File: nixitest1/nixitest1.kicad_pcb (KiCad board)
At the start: 2 copper layers, 22 x 38 mm, 32 parts, among them J1 MSYS, Q1 60V 3A, Q10 HVN, Q11 HVN, Q12 HVN, Q13 HVN, Q2 HVN, Q3 HVN, Q4 HVN, Q5 HVN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

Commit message: Update board design
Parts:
- R1: value 500mΩ -> 10k; footprint Resistor_SMD:R_0805_2012Metric -> Resistor_SMD:R_0402_1005Metric
- moved R1 1.36 mm to (89.0, 65.2), turned to 180 degrees
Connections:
- Q1 pad 2: HVIMON -> GND
- R1 pad 1: HVIMON -> GND
- R1 pad 2: GND -> HVCTL
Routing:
- net HVIMON: track 12.9 -> 0.51 mm, vias 2 -> 0
- net GND: track 172.8 -> 181.8 mm
- net HVCTL: track 7.85 -> 8.91 mm
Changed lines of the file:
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@@
     )
   )
-  (footprint "Resistor_SMD:R_0805_2012Metric" (layer "F.Cu")
-    (at 90.29 64.88)
-    (descr "Resistor SMD 0805 (2012 Metric), square (rectangular) end terminal, IPC_7351 nominal, (Body size source: IPC-SM-782 page 72, https://www.pcb-3d.com/wordpress/wp-content/uploads/ipc-sm-782a_amendment_1_and_2.pdf), generated with kicad-footprint-generator")
+  (footprint "Resistor_SMD:R_0402_1005Metric" (layer "F.Cu")
+    (at 88.97 65.19 180)
+    (descr "Resistor SMD 0402 (1005 Metric), square (rectangular) end terminal, IPC_7351 nominal, (Body size source: IPC-SM-782 page 72, https://www.pcb-3d.com/wordpress/wp-content/uploads/ipc-sm-782a_amendment_1_and_2.pdf), generated with kicad-footprint-generator")
     (tags "resistor")
-    (property "LCSC" "C327217")
-    (property "Sheetfile" "nixitest1.kicad_sch")
-    (property "Sheetname" "")
-    (attr smd)
-    (fp_text reference "R1" (at -2.38 -0.48 unlocked) (layer "F.SilkS")
-      (effects (font (size 0.7 0.7) (thickness 0.1)))
-    )
-    (fp_text value "500mΩ" (at 0 1.65 unlocked) (layer "F.Fab")
+    (property "LCSC" "C25744")
+    (property "Sheetfile" "nixitest1.kicad_sch")
+    (property "Sheetname" "")
+    (attr smd)
+    (fp_text reference "R1" (at -1.73 0.03 unlocked) (layer "F.SilkS")
+      (effects (font (size 0.7 0.7) (thickness 0.1)))
+    )
+    (fp_text value "10k" (at 0 1.17 unlocked) (layer "F.Fab")
       (effects (font (size 1 1) (thickness 0.15)))
     )
@@
       (effects (font (size 1 1) (thickness 0.15)))
     )
-    (fp_line (start -0.227064 -0.735) (end 0.227064 -0.735) (layer "F.SilkS") (width 0.1))
-    (fp_line (start -0.227064 0.735) (end 0.227064 0.735) (layer "F.SilkS") (width 0.1))
-    (fp_line (start -1.68 0.95) (end -1.68 -0.95) (layer "F.CrtYd") (width 0.05))
-    (fp_line (start -1.68 -0.95) (end 1.68 -0.95) (layer "F.CrtYd") (width 0.05))
-    (fp_line (start 1.68 -0.95) (end 1.68 0.95) (layer "F.CrtYd") (width 0.05))
-    (fp_line (start 1.68 0.95) (end -1.68 0.95) (layer "F.CrtYd") (width 0.05))
-    (fp_line (start -1 0.625) (end -1 -0.625) (layer "F.Fab") (width 0.1))
-    (fp_line (start 1 -0.625) (end 1 0.625) (layer "F.Fab") (width 0.1))
-    (fp_line (start 1 0.625) (end -1 0.625) (layer "F.Fab") (width 0.1))
-    (fp_line (start -1 -0.625) (end 1 -0.625) (layer "F.Fab") (width 0.1))
-    (pad "1" smd roundrect locked (at -0.9125 0) (size 1.025 1.4) (layers "F.Cu" "F.Paste" "F.Mask") (roundrect_rratio 0.243902439)
-      (net 5 "HVIMON") (pintype "passive"))
-    (pad "2" smd roundrect locked (at 0.9125 0) (size 1.025 1.4) (layers "F.Cu" "F.Paste" "F.Mask") (roundrect_rratio 0.243902439)
+    (fp_line (start -0.153641 -0.38) (end 0.153641 -0.38) (layer "F.SilkS") (width 0.1))
+    (fp_line (start -0.153641 0.38) (end 0.153641 0.38) (layer "F.SilkS") (width 0.1))
+    (fp_line (start 0.93 0.47) (end -0.93 0.47) (layer "F.CrtYd") (width 0.05))
+    (fp_line (start 0.93 -0.47) (end 0.93 0.47) (layer "F.CrtYd") (width 0.05))
+    (fp_line (start -0.93 -0.47) (end 0.93 -0.47) (layer "F.CrtYd") (width 0.05))
+    (fp_line (start -0.93 0.47) (end -0.93 -0.47) (layer "F.CrtYd") (width 0.05))
+    (fp_line (start 0.525 0.27) (end -0.525 0.27) (layer "F.Fab") (width 0.1))
+    (fp_line (start 0.525 -0.27) (end 0.525 0.27) (layer "F.Fab") (width 0.1))
+    (fp_line (start -0.525 -0.27) (end 0.525 -0.27) (layer "F.Fab") (width 0.1))
+    (fp_line (start -0.525 0.27) (end -0.525 -0.27) (layer "F.Fab") (width 0.1))
+    (pad "1" smd roundrect (at -0.51 0 180) (size 0.54 0.64) (layers "F.Cu" "F.Paste" "F.Mask") (roundrect_rratio 0.25)
       (net 2 "GND") (pintype "passive"))
-    (model "${KICAD6_3DMODEL_DIR}/Resistor_SMD.3dshapes/R_0805_2012Metric.wrl"
+    (pad "2" smd roundrect (at 0.51 0 180) (size 0.54 0.64) (layers "F.Cu" "F.Paste" "F.Mask") (roundrect_rratio 0.25)
+      (net 4 "HVCTL") (pintype "passive"))
+    (model "${KICAD6_3DMODEL_DIR}/Resistor_SMD.3dshapes/R_0402_1005Metric.wrl"
       (offset (xyz 0 0 0))
       (scale (xyz 1 1 1))
@@
       (net 4 "HVCTL") (pinfunction "G") (pintype "input"))
     (pad "2" smd roundrect (at -0.9375 0.95) (size 1.475 0.6) (layers "F.Cu" "F.Paste" "F.Mask") (roundrect_rratio 0.25)
-      (net 5 "HVIMON") (pinfunction "S") (pintype "passive"))
+      (net 2 "GND") (pinfunction "S") (pintype "passive"))
     (pad "3" smd roundrect (at 0.9375 0) (size 1.475 0.6) (layers "F.Cu" "F.Paste" "F.Mask") (roundrect_rratio 0.25)
       (net 6 "Net-(Q1-Pad3)") (pinfunction "D") (pintype "passive"))
@@
   (footprint "IN12-NIXIE:IN12-NIXIE" (layer "F.Cu")
     (at 90 80)
-    (property "LCSC" "~")
+    (property "LCSC" "")
     (property "Sheetfile" "nixitest1.kicad_sch")
     (property "Sheetname" "")
@@
   (gr_arc (start 99 58) (mid 100.414214 58.585786) (end 101 60) (layer "Edge.Cuts") (width 0.1))
   (gr_text "*" (at 87.42 71.84 -120) (layer "B.SilkS")
-    (effects (font (size 1.5 1.5) (thickness 0.15)) (justify mirror))
+    (effects (font (size 0.7 0.7) (thickness 0.1)) (justify mirror))
   )
   (gr_text "GND" (at 85.26 94.31) (layer "F.SilkS")
@@
   )
   (gr_text "*" (at 88.175 71.75 120) (layer "F.SilkS")
-    (effects (font (size 1.5 1.5) (thickness 0.15)))
+    (effects (font (size 0.7 0.7) (thickness 0.1)))
   )
   (gr_text "PGM" (at 94.81 94.35) (layer "F.SilkS")
@@
   (segment (start 82.6 70.975) (end 83.95 71.175) (width 0.2) (layer "F.Cu") (net 2))
   (segment (start 91.307459 58.332541) (end 88.801628 58.328372) (width 0.2) (layer "F.Cu") (net 2))
+  (segment (start 89.48 65.19) (end 90.34 65.33) (width 0.2) (layer "F.Cu") (net 2))
   (segment (start 87.98 82.51) (end 88.2875 84.99) (width 0.2) (layer "F.Cu") (net 2))
   (segment (start 84.925 78.725) (end 85.525 79.225) (width 0.2) (layer "F.Cu") (net 2))
@@
   (segment (start 81.67 81.33) (end 80.925 80.85) (width 0.2) (layer "F.Cu") (net 2))
   (segment (start 84.79 64.075) (end 85.09 63.8) (width 0.2) (layer "F.Cu") (net 2))
+  (segment (start 90.34 65.33) (end 90.65 66.75) (width 0.2) (layer "F.Cu") (net 2))
   (segment (start 93.25 67.15) (end 94.873855 67.098855) (width 0.2) (layer "F.Cu") (net 2))
+  (segment (start 90.65 66.75) (end 90.25 67.2) (width 0.2) (layer "F.Cu") (net 2))
   (segment (start 90.113482 76.523482) (end 91.67 76.35) (width 0.2) (layer "F.Cu") (net 2))
   (segment (start 93.77 85.88) (end 92.0025 85.74) (width 0.2) (layer "F.Cu") (net 2))
@@
   (segment (start 82.9 74.45) (end 82.76 75.32) (width 0.2) (layer "F.Cu") (net 2))
   (segment (start 82.91 75.96) (end 83.9758 78.4758) (width 0.2) (layer "F.Cu") (net 2))
+  (segment (start 90.25 67.2) (end 89.4625 68.5) (width 0.2) (layer "F.Cu") (net 2))
   (segment (start 97.61 79.51) (end 99.0575 81.02) (width 0.2) (layer "F.Cu") (net 2))
   (segment (start 83.52 73.28) (end 84.08 73.92) (width 0.2) (layer "F.Cu") (net 2))
@@
   (segment (start 91.28 58.83) (end 91.305749 58.325749) (width 0.2) (layer "B.Cu") (net 2))
   (segment (start 83.575 63.725) (end 83.225 63.35) (width 0.2) (layer "B.Cu") (net 2))
+  (segment (start 86.975 68.85) (end 85.1 67.25) (width 0.2) (layer "B.Cu") (net 2))
   (segment (start 87.33 63.6) (end 85.09 63.8) (width 0.2) (layer "B.Cu") (net 2))
   (segment (start 85.09 63.8) (end 83.575 63.725) (width 0.2) (layer "B.Cu") (net 2))
@@
   (segment (start 83.375 62.525) (end 84.925 61.65) (width 0.2) (layer "B.Cu") (net 2))
   (segment (start 85.95 66.55) (end 85.09 63.8) (width 0.2) (layer "B.Cu") (net 2))
+  (segment (start 84.825 67.175) (end 83.05 67.475) (width 0.2) (layer "B.Cu") (net 2))
   (segment (start 80.84 58.55) (end 84.67 58.31) (width 0.2) (layer "B.Cu") (net 2))
+  (segment (start 85.1 67.25) (end 84.825 67.175) (width 0.2) (layer "B.Cu") (net 2))
   (segment (start 83.225 63.35) (end 83.375 62.525) (width 0.2) (layer "B.Cu") (net 2))
   (segment (start 88.351263 58.318737) (end 91.305749 58.325749) (width 0.2) (layer "B.Cu") (net 2))
@@
   (segment (start 88.225 66.225) (end 89.4625 66.6) (width 0.2) (layer "F.Cu") (net 4))
   (segment (start 83.41 66.74) (end 83.02 66.81) (width 0.2) (layer "F.Cu") (net 4))
+  (segment (start 88.225 66.225) (end 88.46 65.19) (width 0.2) (layer "F.Cu") (net 4))
   (segment (start 83.909999 66.74) (end 83.41 66.74) (width 0.2) (layer "F.Cu") (net 4))
   (via (at 88.225 66.225) (size 0.5) (drill 0.25) (layers "F.Cu" "B.Cu") (net 4))
@@
   (segment (start 87.925 66.65) (end 88.225 66.225) (width 0.2) (layer "B.Cu") (net 4))
   (segment (start 85.75 67.125) (end 86.325 67.2) (width 0.2) (layer "B.Cu") (net 4))
-  (segment (start 89.3375 64.65) (end 90.65 65.85) (width 0.2) (layer "F.Cu") (net 5))
   (segment (start 83.909999 67.14) (end 83.4 67.15) (width 0.2) (layer "F.Cu") (net 5))
-  (segment (start 83.4 67.15) (end 83.05 67.475) (width 0.2) (layer "F.Cu") (net 5))
-  (segment (start 90.25 67.2) (end 89.4625 68.5) (width 0.2) (layer "F.Cu") (net 5))
-  (segment (start 86.975 68.85) (end 89.4625 68.5) (width 0.2) (layer "F.Cu") (net 5))
-  (segment (start 90.65 65.85) (end 90.65 66.75) (width 0.2) (layer "F.Cu") (net 5))
-  (segment (start 90.65 66.75) (end 90.25 67.2) (width 0.2) (layer "F.Cu") (net 5))
-  (via (at 83.05 67.475) (size 0.5) (drill 0.25) (layers "F.Cu" "B.Cu") (net 5))
-  (via (at 86.975 68.85) (size 0.5) (drill 0.25) (layers "F.Cu" "B.Cu") (net 5))
-  (segment (start 86.975 68.85) (end 85.1 67.25) (width 0.2) (layer "B.Cu") (net 5))
-  (segment (start 84.825 67.175) (end 83.05 67.475) (width 0.2) (layer "B.Cu") (net 5))
-  (segment (start 85.1 67.25) (end 84.825 67.175) (width 0.2) (layer "B.Cu") (net 5))
   (segment (start 91.3375 67.55) (end 93.065 68.9) (width 0.2) (layer "F.Cu") (net 6))
   (segment (start 85.66 78.42) (end 86.8875 78.62) (width 0.2) (layer "F.Cu") (net 7))

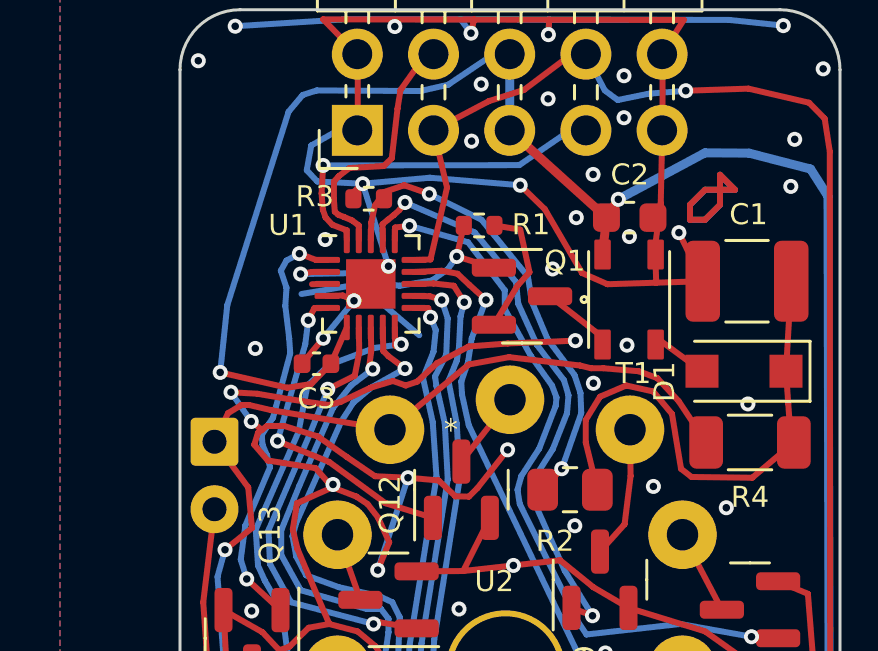
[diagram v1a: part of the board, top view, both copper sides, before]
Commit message: * Revert pcb so it matches production files. * Move original thoughts into attic. * Update comments on firmware
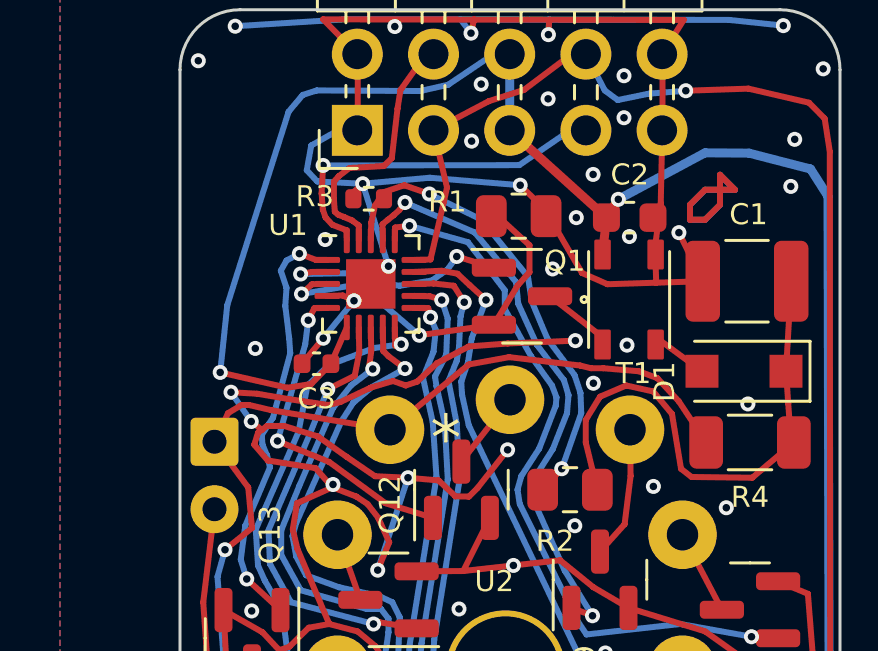
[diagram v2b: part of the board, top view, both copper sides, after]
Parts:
- R1: value 10k -> 500mΩ; footprint Resistor_SMD:R_0402_1005Metric -> Resistor_SMD:R_0805_2012Metric
- moved R1 1.36 mm to (90.3, 64.9), turned to 0 degrees
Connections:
- Q1 pad 2: GND -> HVIMON
- R1 pad 1: GND -> HVIMON
- R1 pad 2: HVCTL -> GND
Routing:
- net HVIMON: track 0.51 -> 12.9 mm, vias 0 -> 2
- net GND: track 181.8 -> 172.8 mm
- net HVCTL: track 8.91 -> 7.85 mm
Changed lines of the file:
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@@
     )
   )
-  (footprint "Resistor_SMD:R_0402_1005Metric" (layer "F.Cu")
-    (at 88.97 65.19 180)
-    (descr "Resistor SMD 0402 (1005 Metric), square (rectangular) end terminal, IPC_7351 nominal, (Body size source: IPC-SM-782 page 72, https://www.pcb-3d.com/wordpress/wp-content/uploads/ipc-sm-782a_amendment_1_and_2.pdf), generated with kicad-footprint-generator")
+  (footprint "Resistor_SMD:R_0805_2012Metric" (layer "F.Cu")
+    (at 90.29 64.88)
+    (descr "Resistor SMD 0805 (2012 Metric), square (rectangular) end terminal, IPC_7351 nominal, (Body size source: IPC-SM-782 page 72, https://www.pcb-3d.com/wordpress/wp-content/uploads/ipc-sm-782a_amendment_1_and_2.pdf), generated with kicad-footprint-generator")
     (tags "resistor")
-    (property "LCSC" "C25744")
-    (property "Sheetfile" "nixitest1.kicad_sch")
-    (property "Sheetname" "")
-    (attr smd)
-    (fp_text reference "R1" (at -1.73 0.03 unlocked) (layer "F.SilkS")
-      (effects (font (size 0.7 0.7) (thickness 0.1)))
-    )
-    (fp_text value "10k" (at 0 1.17 unlocked) (layer "F.Fab")
+    (property "LCSC" "C327217")
+    (property "Sheetfile" "nixitest1.kicad_sch")
+    (property "Sheetname" "")
+    (attr smd)
+    (fp_text reference "R1" (at -2.38 -0.48 unlocked) (layer "F.SilkS")
+      (effects (font (size 0.7 0.7) (thickness 0.1)))
+    )
+    (fp_text value "500mΩ" (at 0 1.65 unlocked) (layer "F.Fab")
       (effects (font (size 1 1) (thickness 0.15)))
     )
@@
       (effects (font (size 1 1) (thickness 0.15)))
     )
-    (fp_line (start -0.153641 -0.38) (end 0.153641 -0.38) (layer "F.SilkS") (width 0.1))
-    (fp_line (start -0.153641 0.38) (end 0.153641 0.38) (layer "F.SilkS") (width 0.1))
-    (fp_line (start 0.93 0.47) (end -0.93 0.47) (layer "F.CrtYd") (width 0.05))
-    (fp_line (start 0.93 -0.47) (end 0.93 0.47) (layer "F.CrtYd") (width 0.05))
-    (fp_line (start -0.93 -0.47) (end 0.93 -0.47) (layer "F.CrtYd") (width 0.05))
-    (fp_line (start -0.93 0.47) (end -0.93 -0.47) (layer "F.CrtYd") (width 0.05))
-    (fp_line (start 0.525 0.27) (end -0.525 0.27) (layer "F.Fab") (width 0.1))
-    (fp_line (start 0.525 -0.27) (end 0.525 0.27) (layer "F.Fab") (width 0.1))
-    (fp_line (start -0.525 -0.27) (end 0.525 -0.27) (layer "F.Fab") (width 0.1))
-    (fp_line (start -0.525 0.27) (end -0.525 -0.27) (layer "F.Fab") (width 0.1))
-    (pad "1" smd roundrect (at -0.51 0 180) (size 0.54 0.64) (layers "F.Cu" "F.Paste" "F.Mask") (roundrect_rratio 0.25)
+    (fp_line (start -0.227064 -0.735) (end 0.227064 -0.735) (layer "F.SilkS") (width 0.1))
+    (fp_line (start -0.227064 0.735) (end 0.227064 0.735) (layer "F.SilkS") (width 0.1))
+    (fp_line (start -1.68 0.95) (end -1.68 -0.95) (layer "F.CrtYd") (width 0.05))
+    (fp_line (start -1.68 -0.95) (end 1.68 -0.95) (layer "F.CrtYd") (width 0.05))
+    (fp_line (start 1.68 -0.95) (end 1.68 0.95) (layer "F.CrtYd") (width 0.05))
+    (fp_line (start 1.68 0.95) (end -1.68 0.95) (layer "F.CrtYd") (width 0.05))
+    (fp_line (start -1 0.625) (end -1 -0.625) (layer "F.Fab") (width 0.1))
+    (fp_line (start 1 -0.625) (end 1 0.625) (layer "F.Fab") (width 0.1))
+    (fp_line (start 1 0.625) (end -1 0.625) (layer "F.Fab") (width 0.1))
+    (fp_line (start -1 -0.625) (end 1 -0.625) (layer "F.Fab") (width 0.1))
+    (pad "1" smd roundrect locked (at -0.9125 0) (size 1.025 1.4) (layers "F.Cu" "F.Paste" "F.Mask") (roundrect_rratio 0.243902439)
+      (net 5 "HVIMON") (pintype "passive"))
+    (pad "2" smd roundrect locked (at 0.9125 0) (size 1.025 1.4) (layers "F.Cu" "F.Paste" "F.Mask") (roundrect_rratio 0.243902439)
       (net 2 "GND") (pintype "passive"))
-    (pad "2" smd roundrect (at 0.51 0 180) (size 0.54 0.64) (layers "F.Cu" "F.Paste" "F.Mask") (roundrect_rratio 0.25)
-      (net 4 "HVCTL") (pintype "passive"))
-    (model "${KICAD6_3DMODEL_DIR}/Resistor_SMD.3dshapes/R_0402_1005Metric.wrl"
+    (model "${KICAD6_3DMODEL_DIR}/Resistor_SMD.3dshapes/R_0805_2012Metric.wrl"
       (offset (xyz 0 0 0))
       (scale (xyz 1 1 1))
@@
       (net 4 "HVCTL") (pinfunction "G") (pintype "input"))
     (pad "2" smd roundrect (at -0.9375 0.95) (size 1.475 0.6) (layers "F.Cu" "F.Paste" "F.Mask") (roundrect_rratio 0.25)
-      (net 2 "GND") (pinfunction "S") (pintype "passive"))
+      (net 5 "HVIMON") (pinfunction "S") (pintype "passive"))
     (pad "3" smd roundrect (at 0.9375 0) (size 1.475 0.6) (layers "F.Cu" "F.Paste" "F.Mask") (roundrect_rratio 0.25)
       (net 6 "Net-(Q1-Pad3)") (pinfunction "D") (pintype "passive"))
@@
   (footprint "IN12-NIXIE:IN12-NIXIE" (layer "F.Cu")
     (at 90 80)
-    (property "LCSC" "")
+    (property "LCSC" "~")
     (property "Sheetfile" "nixitest1.kicad_sch")
     (property "Sheetname" "")
@@
   (gr_arc (start 99 58) (mid 100.414214 58.585786) (end 101 60) (layer "Edge.Cuts") (width 0.1))
   (gr_text "*" (at 87.42 71.84 -120) (layer "B.SilkS")
-    (effects (font (size 0.7 0.7) (thickness 0.1)) (justify mirror))
+    (effects (font (size 1.5 1.5) (thickness 0.15)) (justify mirror))
   )
   (gr_text "GND" (at 85.26 94.31) (layer "F.SilkS")
@@
   )
   (gr_text "*" (at 88.175 71.75 120) (layer "F.SilkS")
-    (effects (font (size 0.7 0.7) (thickness 0.1)))
+    (effects (font (size 1.5 1.5) (thickness 0.15)))
   )
   (gr_text "PGM" (at 94.81 94.35) (layer "F.SilkS")
@@
   (segment (start 82.6 70.975) (end 83.95 71.175) (width 0.2) (layer "F.Cu") (net 2))
   (segment (start 91.307459 58.332541) (end 88.801628 58.328372) (width 0.2) (layer "F.Cu") (net 2))
-  (segment (start 89.48 65.19) (end 90.34 65.33) (width 0.2) (layer "F.Cu") (net 2))
   (segment (start 87.98 82.51) (end 88.2875 84.99) (width 0.2) (layer "F.Cu") (net 2))
   (segment (start 84.925 78.725) (end 85.525 79.225) (width 0.2) (layer "F.Cu") (net 2))
@@
   (segment (start 81.67 81.33) (end 80.925 80.85) (width 0.2) (layer "F.Cu") (net 2))
   (segment (start 84.79 64.075) (end 85.09 63.8) (width 0.2) (layer "F.Cu") (net 2))
-  (segment (start 90.34 65.33) (end 90.65 66.75) (width 0.2) (layer "F.Cu") (net 2))
   (segment (start 93.25 67.15) (end 94.873855 67.098855) (width 0.2) (layer "F.Cu") (net 2))
-  (segment (start 90.65 66.75) (end 90.25 67.2) (width 0.2) (layer "F.Cu") (net 2))
   (segment (start 90.113482 76.523482) (end 91.67 76.35) (width 0.2) (layer "F.Cu") (net 2))
   (segment (start 93.77 85.88) (end 92.0025 85.74) (width 0.2) (layer "F.Cu") (net 2))
@@
   (segment (start 82.9 74.45) (end 82.76 75.32) (width 0.2) (layer "F.Cu") (net 2))
   (segment (start 82.91 75.96) (end 83.9758 78.4758) (width 0.2) (layer "F.Cu") (net 2))
-  (segment (start 90.25 67.2) (end 89.4625 68.5) (width 0.2) (layer "F.Cu") (net 2))
   (segment (start 97.61 79.51) (end 99.0575 81.02) (width 0.2) (layer "F.Cu") (net 2))
   (segment (start 83.52 73.28) (end 84.08 73.92) (width 0.2) (layer "F.Cu") (net 2))
@@
   (segment (start 91.28 58.83) (end 91.305749 58.325749) (width 0.2) (layer "B.Cu") (net 2))
   (segment (start 83.575 63.725) (end 83.225 63.35) (width 0.2) (layer "B.Cu") (net 2))
-  (segment (start 86.975 68.85) (end 85.1 67.25) (width 0.2) (layer "B.Cu") (net 2))
   (segment (start 87.33 63.6) (end 85.09 63.8) (width 0.2) (layer "B.Cu") (net 2))
   (segment (start 85.09 63.8) (end 83.575 63.725) (width 0.2) (layer "B.Cu") (net 2))
@@
   (segment (start 83.375 62.525) (end 84.925 61.65) (width 0.2) (layer "B.Cu") (net 2))
   (segment (start 85.95 66.55) (end 85.09 63.8) (width 0.2) (layer "B.Cu") (net 2))
-  (segment (start 84.825 67.175) (end 83.05 67.475) (width 0.2) (layer "B.Cu") (net 2))
   (segment (start 80.84 58.55) (end 84.67 58.31) (width 0.2) (layer "B.Cu") (net 2))
-  (segment (start 85.1 67.25) (end 84.825 67.175) (width 0.2) (layer "B.Cu") (net 2))
   (segment (start 83.225 63.35) (end 83.375 62.525) (width 0.2) (layer "B.Cu") (net 2))
   (segment (start 88.351263 58.318737) (end 91.305749 58.325749) (width 0.2) (layer "B.Cu") (net 2))
@@
   (segment (start 88.225 66.225) (end 89.4625 66.6) (width 0.2) (layer "F.Cu") (net 4))
   (segment (start 83.41 66.74) (end 83.02 66.81) (width 0.2) (layer "F.Cu") (net 4))
-  (segment (start 88.225 66.225) (end 88.46 65.19) (width 0.2) (layer "F.Cu") (net 4))
   (segment (start 83.909999 66.74) (end 83.41 66.74) (width 0.2) (layer "F.Cu") (net 4))
   (via (at 88.225 66.225) (size 0.5) (drill 0.25) (layers "F.Cu" "B.Cu") (net 4))
@@
   (segment (start 87.925 66.65) (end 88.225 66.225) (width 0.2) (layer "B.Cu") (net 4))
   (segment (start 85.75 67.125) (end 86.325 67.2) (width 0.2) (layer "B.Cu") (net 4))
+  (segment (start 89.3375 64.65) (end 90.65 65.85) (width 0.2) (layer "F.Cu") (net 5))
   (segment (start 83.909999 67.14) (end 83.4 67.15) (width 0.2) (layer "F.Cu") (net 5))
+  (segment (start 83.4 67.15) (end 83.05 67.475) (width 0.2) (layer "F.Cu") (net 5))
+  (segment (start 90.25 67.2) (end 89.4625 68.5) (width 0.2) (layer "F.Cu") (net 5))
+  (segment (start 86.975 68.85) (end 89.4625 68.5) (width 0.2) (layer "F.Cu") (net 5))
+  (segment (start 90.65 65.85) (end 90.65 66.75) (width 0.2) (layer "F.Cu") (net 5))
+  (segment (start 90.65 66.75) (end 90.25 67.2) (width 0.2) (layer "F.Cu") (net 5))
+  (via (at 83.05 67.475) (size 0.5) (drill 0.25) (layers "F.Cu" "B.Cu") (net 5))
+  (via (at 86.975 68.85) (size 0.5) (drill 0.25) (layers "F.Cu" "B.Cu") (net 5))
+  (segment (start 86.975 68.85) (end 85.1 67.25) (width 0.2) (layer "B.Cu") (net 5))
+  (segment (start 84.825 67.175) (end 83.05 67.475) (width 0.2) (layer "B.Cu") (net 5))
+  (segment (start 85.1 67.25) (end 84.825 67.175) (width 0.2) (layer "B.Cu") (net 5))
   (segment (start 91.3375 67.55) (end 93.065 68.9) (width 0.2) (layer "F.Cu") (net 6))
   (segment (start 85.66 78.42) (end 86.8875 78.62) (width 0.2) (layer "F.Cu") (net 7))
